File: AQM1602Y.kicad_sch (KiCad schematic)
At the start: 9 parts, among them J11 LCD, J12 LCD_BackLight

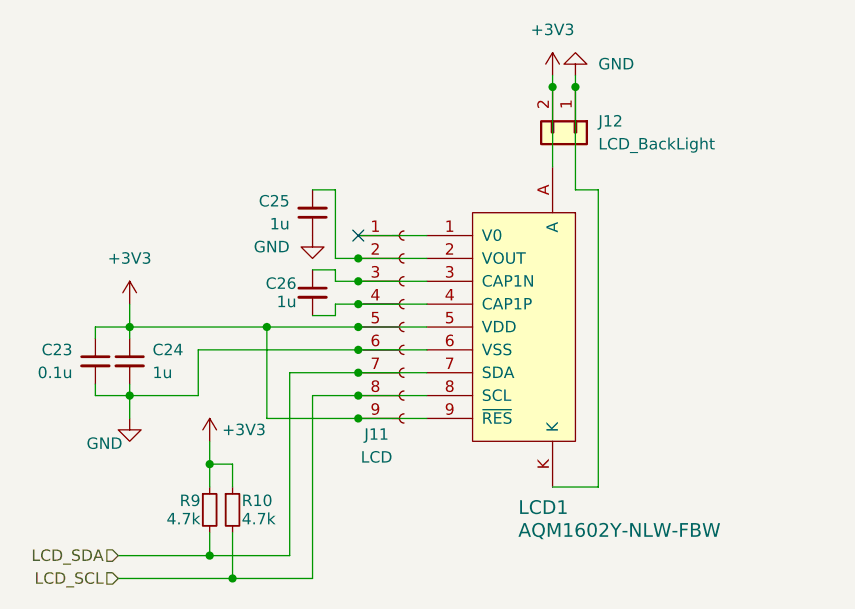
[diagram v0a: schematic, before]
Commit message: CANの終端抵抗を削除、シルクスクリーンを調整
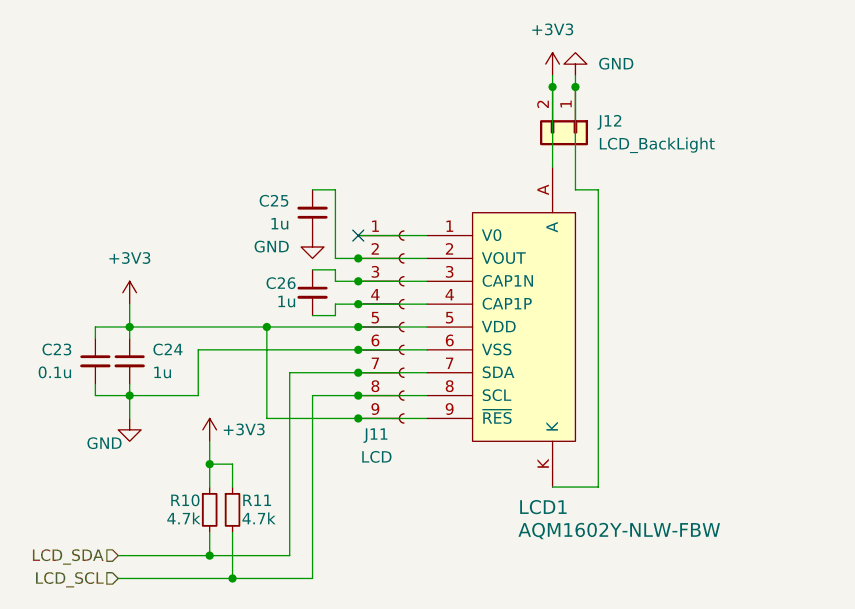
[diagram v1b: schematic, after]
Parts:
- renumbered R9 to R10, R10 to R11
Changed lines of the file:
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@@
 		(dnp no)
 		(fields_autoplaced yes)
-		(property "Reference" "#PWR057"
+		(property "Reference" "#PWR059"
 			(at 176.53 76.2 0)
 			(effects
@@
 			(project "DRC-CCTL2026"
 				(path "/5b9f915a-dea8-4ee6-a342-61437447bbca/3d8d4604-9990-4cd6-b941-b64af6e081cc"
-					(reference "#PWR057")
+					(reference "#PWR059")
 					(unit 1)
 				)
@@
 		(dnp no)
 		(fields_autoplaced yes)
-		(property "Reference" "#PWR058"
+		(property "Reference" "#PWR060"
 			(at 179.07 66.04 0)
 			(effects
@@
 			(project "DRC-CCTL2026"
 				(path "/5b9f915a-dea8-4ee6-a342-61437447bbca/3d8d4604-9990-4cd6-b941-b64af6e081cc"
-					(reference "#PWR058")
+					(reference "#PWR060")
 					(unit 1)
 				)
@@
 		(on_board yes)
 		(dnp no)
-		(property "Reference" "#PWR054"
+		(property "Reference" "#PWR056"
 			(at 129.54 116.84 0)
 			(effects
@@
 			(project "DRC-CCTL2026"
 				(path "/5b9f915a-dea8-4ee6-a342-61437447bbca/3d8d4604-9990-4cd6-b941-b64af6e081cc"
-					(reference "#PWR054")
+					(reference "#PWR056")
 					(unit 1)
 				)
@@
 		(on_board yes)
 		(dnp no)
-		(property "Reference" "#PWR055"
+		(property "Reference" "#PWR057"
 			(at 138.43 116.84 0)
 			(effects
@@
 			(project "DRC-CCTL2026"
 				(path "/5b9f915a-dea8-4ee6-a342-61437447bbca/3d8d4604-9990-4cd6-b941-b64af6e081cc"
-					(reference "#PWR055")
+					(reference "#PWR057")
 					(unit 1)
 				)
@@
 		(on_board yes)
 		(dnp no)
-		(property "Reference" "R10"
+		(property "Reference" "R11"
 			(at 141.986 119.634 0)
 			(effects
@@
 			(project "DRC-CCTL2026"
 				(path "/5b9f915a-dea8-4ee6-a342-61437447bbca/3d8d4604-9990-4cd6-b941-b64af6e081cc"
-					(reference "R10")
+					(reference "R11")
 					(unit 1)
 				)
@@
 		(dnp no)
 		(fields_autoplaced yes)
-		(property "Reference" "#PWR053"
+		(property "Reference" "#PWR055"
 			(at 129.54 101.6 0)
 			(effects
@@
 			(project "DRC-CCTL2026"
 				(path "/5b9f915a-dea8-4ee6-a342-61437447bbca/3d8d4604-9990-4cd6-b941-b64af6e081cc"
-					(reference "#PWR053")
+					(reference "#PWR055")
 					(unit 1)
 				)
@@
 		(dnp no)
 		(fields_autoplaced yes)
-		(property "Reference" "#PWR056"
+		(property "Reference" "#PWR058"
 			(at 149.86 96.52 0)
 			(effects
@@
 			(project "DRC-CCTL2026"
 				(path "/5b9f915a-dea8-4ee6-a342-61437447bbca/3d8d4604-9990-4cd6-b941-b64af6e081cc"
-					(reference "#PWR056")
+					(reference "#PWR058")
 					(unit 1)
 				)
@@
 		(on_board yes)
 		(dnp no)
-		(property "Reference" "R9"
+		(property "Reference" "R10"
 			(at 137.414 119.634 0)
 			(effects
@@
 			(project "DRC-CCTL2026"
 				(path "/5b9f915a-dea8-4ee6-a342-61437447bbca/3d8d4604-9990-4cd6-b941-b64af6e081cc"
-					(reference "R9")
-					(unit 1)
-				)
+					(reference "R10")
+					(unit 1)
+				)

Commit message: v0.2.0
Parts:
- removed J11: LCD, Connector_PinSocket_2.54mm:PinSocket_1x09_P2.54mm_Vertical, symbol Connector:Conn_01x09_Socket
- removed J12: LCD_BackLight, Connector_JST:JST_XH_B2B-XH-A_1x02_P2.50mm_Vertical, symbol Connector_Generic:Conn_01x02
- added SW2: SS-12D00G3, lib:SS-12D00G3, symbol Switch:SW_SPDT
- renumbered C24 to C10, C25 to C11, C26 to C12, C23 to C9
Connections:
- net +3V3: now also SW2.1 (A); no longer LCD1.A
- net GND: now also SW2.3 (C)
- new net: LCD1.A, SW2.2 (B)
